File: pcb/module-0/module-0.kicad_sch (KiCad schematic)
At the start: 28 parts, among them J1 Conn_01x06, J2 Conn_01x06, SW1 SW_Push, SW2 SW_Push, SW3 SW_Push, SW4 SW_Push, SW5 RotaryEncoder_Switch_MP, U1 ESP32 S3 L, U2 MCP23S17_SO, U3 74AHC541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

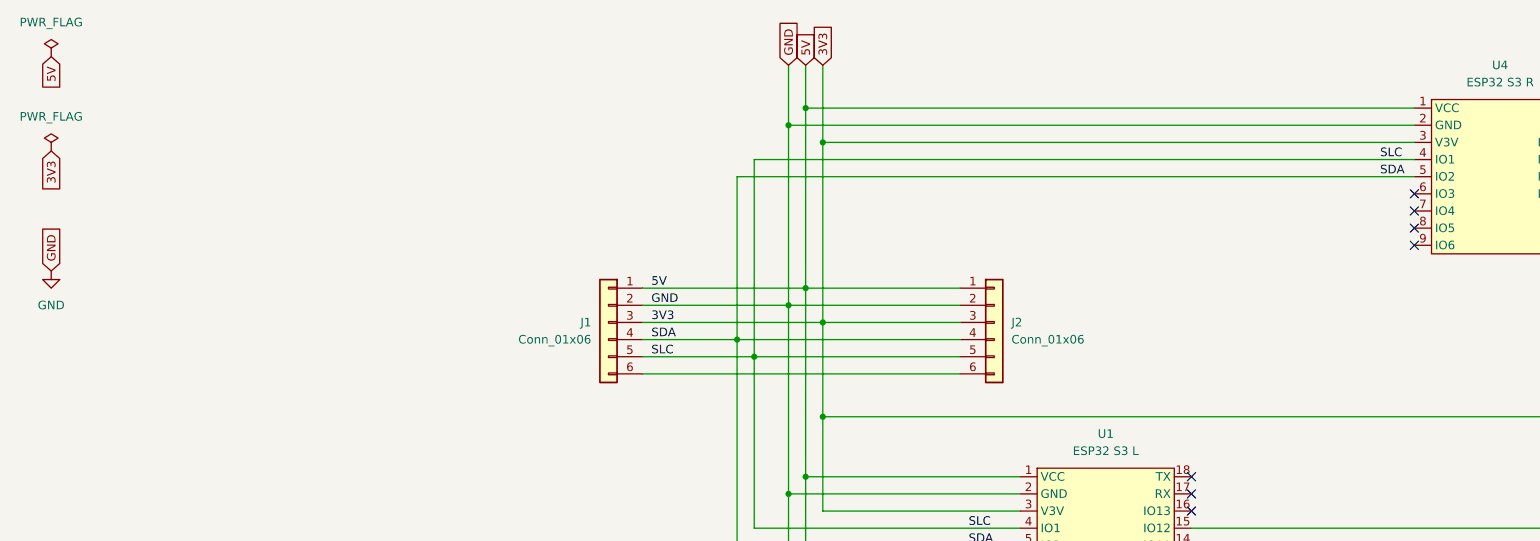
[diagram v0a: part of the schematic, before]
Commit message: 3V net should not be shared across the bus
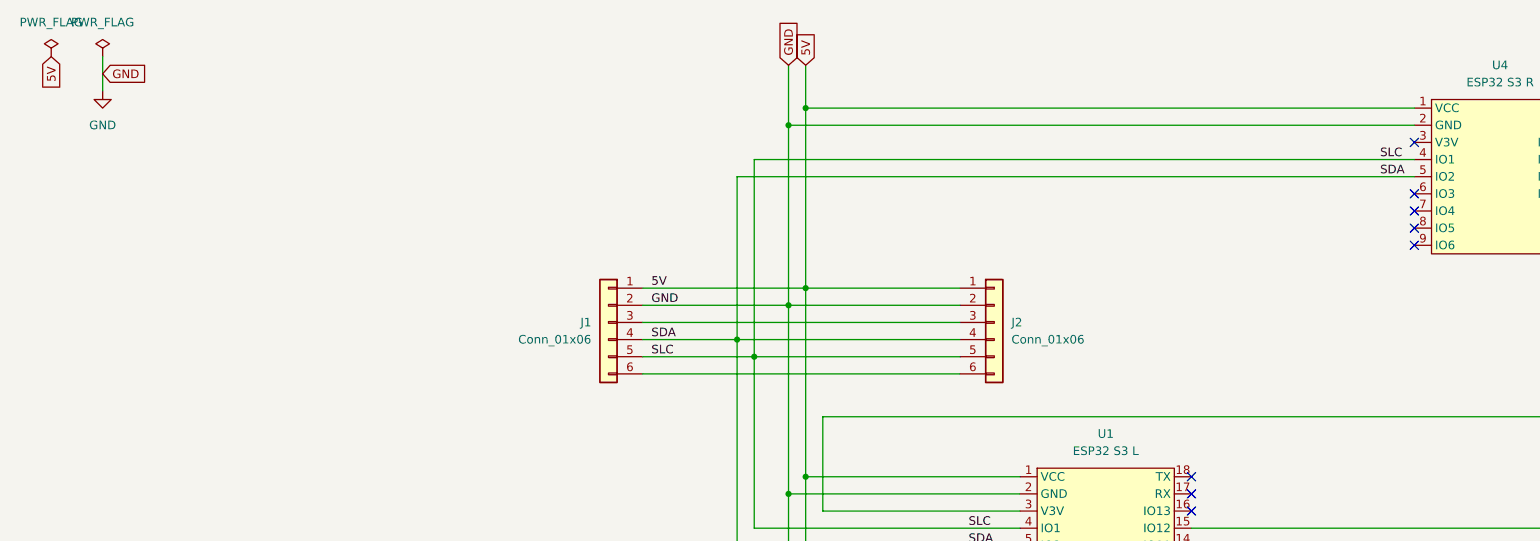
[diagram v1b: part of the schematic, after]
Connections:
- net 3V3: no longer J1.3 (Pin_3), J2.3 (Pin_3), U4.3 (V3V)
- new net: J1.3 (Pin_3), J2.3 (Pin_3)
- no-connect marks 35 -> 36
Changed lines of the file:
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@@
 	)
 	(junction
-		(at 134.62 59.69)
-		(diameter 0)
-		(color 0 0 0 0)
-	)
-	(junction
 		(at 365.76 124.46)
 		(diameter 0)
@@
 	)
 	(junction
-		(at 134.62 33.02)
-		(diameter 0)
-		(color 0 0 0 0)
-	)
-	(junction
-		(at 134.62 73.66)
-		(diameter 0)
-		(color 0 0 0 0)
-	)
-	(junction
 		(at 424.18 162.56)
 		(diameter 0)
@@
 	)
 	(no_connect
+		(at 222.25 33.02)
+	)
+	(no_connect
 		(at 247.65 45.72)
 	)
@@
 	(wire
 		(pts
-			(xy 107.95 59.69) (xy 134.62 59.69)
-		)
-		(stroke
-			(width 0)
-			(type default)
-		)
-	)
-	(wire
-		(pts
 			(xy 292.1 58.42) (xy 292.1 109.22)
 		)
@@
 	(wire
 		(pts
-			(xy 134.62 59.69) (xy 154.94 59.69)
-		)
-		(stroke
-			(width 0)
-			(type default)
-		)
-	)
-	(wire
-		(pts
 			(xy 369.57 163.83) (xy 369.57 154.94)
 		)
@@
 	(wire
 		(pts
-			(xy 134.62 33.02) (xy 134.62 59.69)
-		)
-		(stroke
-			(width 0)
-			(type default)
-		)
-	)
-	(wire
-		(pts
 			(xy 339.09 114.3) (xy 339.09 91.44)
 		)
@@
 	(wire
 		(pts
+			(xy 107.95 59.69) (xy 154.94 59.69)
+		)
+		(stroke
+			(width 0)
+			(type default)
+		)
+	)
+	(wire
+		(pts
 			(xy 392.43 147.32) (xy 424.18 147.32)
 		)
@@
 	(wire
 		(pts
-			(xy 134.62 33.02) (xy 222.25 33.02)
-		)
-		(stroke
-			(width 0)
-			(type default)
-		)
-	)
-	(wire
-		(pts
 			(xy 121.92 38.1) (xy 222.25 38.1)
 		)
@@
 	(wire
 		(pts
-			(xy 134.62 21.59) (xy 134.62 33.02)
-		)
-		(stroke
-			(width 0)
-			(type default)
-		)
-	)
-	(wire
-		(pts
 			(xy 383.54 162.56) (xy 383.54 193.04)
 		)
@@
 	(wire
 		(pts
-			(xy 129.54 135.89) (xy 287.02 135.89)
+			(xy 27.94 20.32) (xy 27.94 25.4)
 		)
 		(stroke
@@
 	(wire
 		(pts
-			(xy 134.62 59.69) (xy 134.62 73.66)
+			(xy 129.54 135.89) (xy 287.02 135.89)
 		)
 		(stroke
@@
 		)
 	)
-	(label "3V3"
-		(at 109.22 59.69 0)
-		(effects
-			(font
-				(size 1.27 1.27)
-			)
-			(justify left bottom)
-		)
-	)
 	(label "SDA"
 		(at 109.22 62.23 0)
@@
 	(global_label "GND"
 		(shape input)
-		(at 20.32 52.07 90)
-		(fields_autoplaced yes)
-		(effects
-			(font
-				(size 1.27 1.27)
-			)
-			(justify left)
-		)
-		(property "Intersheetrefs" "${INTERSHEET_REFS}"
-			(at 20.32 45.2143 90)
-			(effects
-				(font
-					(size 1.27 1.27)
-				)
-				(justify left)
-				(hide yes)
-			)
-		)
-	)
-	(global_label "3V3"
-		(shape input)
-		(at 134.62 21.59 90)
+		(at 27.94 22.86 0)
 		(fields_autoplaced yes)
 		(effects
@@
 		)
 		(property "Intersheetrefs" "${INTERSHEET_REFS}"
-			(at 134.62 15.0972 90)
+			(at 34.7957 22.86 0)
 			(effects
 				(font
@@
 		)
 	)
-	(global_label "3V3"
-		(shape input)
-		(at 20.32 34.29 270)
-		(fields_autoplaced yes)
-		(effects
-			(font
-				(size 1.27 1.27)
-			)
-			(justify right)
-		)
-		(property "Intersheetrefs" "${INTERSHEET_REFS}"
-			(at 20.32 40.7828 90)
-			(effects
-				(font
-					(size 1.27 1.27)
-				)
-				(justify right)
-				(hide yes)
-			)
-		)
-	)
 	(global_label "GND"
 		(shape input)
@@
 	)
 	(symbol
+		(lib_id "power:PWR_FLAG")
+		(at 27.94 20.32 0)
+		(unit 1)
+		(exclude_from_sim no)
+		(in_bom yes)
+		(on_board yes)
+		(dnp no)
+		(fields_autoplaced yes)
+		(property "Reference" "#FLG02"
+			(at 27.94 18.415 0)
+			(effects
+				(font
+					(size 1.27 1.27)
+				)
+				(hide yes)
+			)
+		)
+		(property "Value" "PWR_FLAG"
+			(at 27.94 15.24 0)
+			(effects
+				(font
+					(size 1.27 1.27)
+				)
+			)
+		)
+		(property "Footprint" ""
+			(at 27.94 20.32 0)
+			(effects
+				(font
+					(size 1.27 1.27)
+				)
+				(hide yes)
+			)
+		)
+		(property "Datasheet" "~"
+			(at 27.94 20.32 0)
+			(effects
+				(font
+					(size 1.27 1.27)
+				)
+				(hide yes)
+			)
+		)
+		(property "Description" "Special symbol for telling ERC where power comes from"
+			(at 27.94 20.32 0)
+			(effects
+				(font
+					(size 1.27 1.27)
+				)
+				(hide yes)
+			)
+		)
+		(pin "1"
+		)
+		(instances
+			(project ""
+				(path "/0888bf04-c6c1-4923-af80-2189ee3798b4"
+					(reference "#FLG02")
+					(unit 1)
+				)
+			)
+		)
+	)
+	(symbol
 		(lib_id "Mechanical:MountingHole")
 		(at 34.29 135.89 0)
@@
 	)
 	(symbol
-		(lib_id "power:PWR_FLAG")
-		(at 20.32 34.29 0)
-		(unit 1)
-		(exclude_from_sim no)
-		(in_bom yes)
-		(on_board yes)
-		(dnp no)
-		(fields_autoplaced yes)
-		(property "Reference" "#FLG02"
-			(at 20.32 32.385 0)
-			(effects
-				(font
-					(size 1.27 1.27)
-				)
-				(hide yes)
-			)
-		)
-		(property "Value" "PWR_FLAG"
-			(at 20.32 29.21 0)
-			(effects
-				(font
-					(size 1.27 1.27)
-				)
-			)
-		)
-		(property "Footprint" ""
-			(at 20.32 34.29 0)
-			(effects
-				(font
-					(size 1.27 1.27)
-				)
-				(hide yes)
-			)
-		)
-		(property "Datasheet" "~"
-			(at 20.32 34.29 0)
-			(effects
-				(font
-					(size 1.27 1.27)
-				)
-				(hide yes)
-			)
-		)
-		(property "Description" "Special symbol for telling ERC where power comes from"
-			(at 20.32 34.29 0)
-			(effects
-				(font
-					(size 1.27 1.27)
-				)
-				(hide yes)
-			)
-		)
-		(pin "1"
-		)
-		(instances
-			(project "modular-key-pad"
-				(path "/0888bf04-c6c1-4923-af80-2189ee3798b4"
-					(reference "#FLG02")
-					(unit 1)
-				)
-			)
-		)
-	)
-	(symbol
 		(lib_id "Switch:SW_Push")
 		(at 474.98 78.74 270)
@@
 	(symbol
 		(lib_id "power:GND")
-		(at 20.32 52.07 0)
+		(at 27.94 25.4 0)
 		(unit 1)
 		(exclude_from_sim no)
@@
 		(fields_autoplaced yes)
 		(property "Reference" "#PWR01"
-			(at 20.32 58.42 0)
+			(at 27.94 31.75 0)
 			(effects
 				(font
@@
 		)
 		(property "Value" "GND"
-			(at 20.32 57.15 0)
+			(at 27.94 30.48 0)
 			(effects
 				(font
@@
 		)
 		(property "Footprint" ""
-			(at 20.32 52.07 0)
+			(at 27.94 25.4 0)
 			(effects
 				(font
@@
 		)
 		(property "Datasheet" ""
-			(at 20.32 52.07 0)
+			(at 27.94 25.4 0)
 			(effects
 				(font
@@
 		)
 		(property "Description" "Power symbol creates a global label with name \"GND\" , ground"
-			(at 20.32 52.07 0)
+			(at 27.94 25.4 0)
 			(effects
 				(font

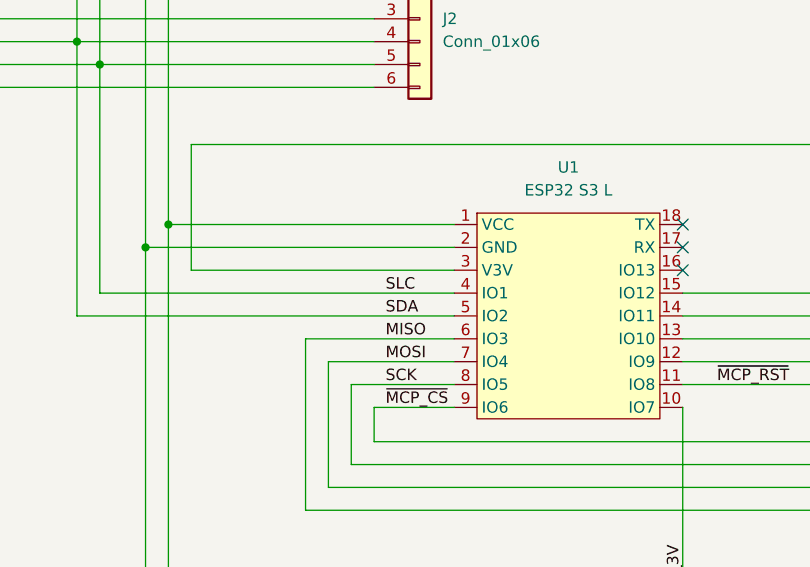
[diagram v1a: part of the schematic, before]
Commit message: Refactor firmware construction
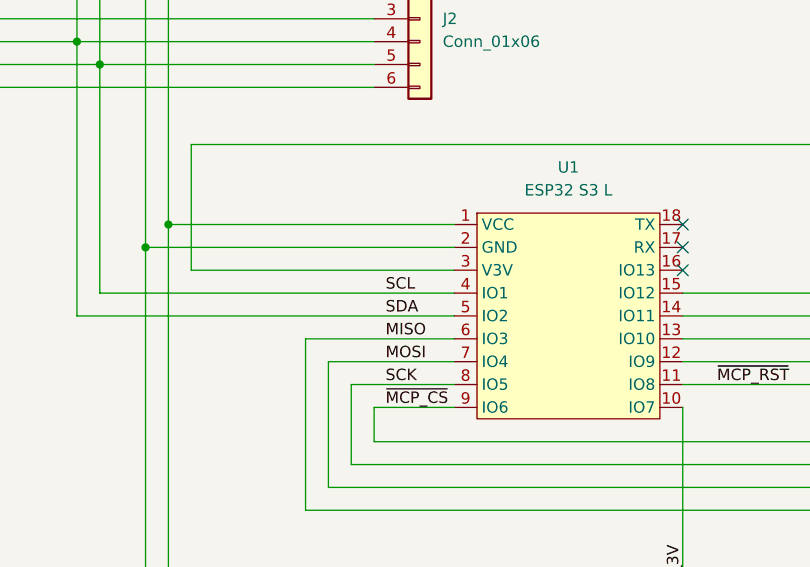
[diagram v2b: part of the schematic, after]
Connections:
- net SLC renamed SCL
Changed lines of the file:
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@@
 		)
 	)
-	(label "SLC"
+	(label "SCL"
 		(at 156.21 90.17 0)
 		(effects
